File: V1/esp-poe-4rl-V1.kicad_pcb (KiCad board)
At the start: 4 copper layers, 82.5 x 45 mm, 105 parts, among them J1 USB_C_Receptacle_USB2.0, J2 250-202, J3 RJ45 JACK, J4 250-202, K1 G5NB-1A-E-DC5, K2 G5NB-1A-E-DC5, Q1 UMH3N, Q2 MMBT2222A, Q3 WPM2015-3/TR, Q4 LMUN2211LT1G, Q5 MMBT2222A, SW1 RESET, U1 CH340K, U2 ESP32-WROOM-32UE-N16, U3 LAN8710A, U4 TPS2376DDAR-H, U5 TX4138, U6 SY8089A1AAC

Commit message: Under development.
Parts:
- added D12: WHITE, Tales:LED_0603_1608Metric, F.Cu at (71.6, 59.1)
- added D13: WHITE, Tales:LED_0603_1608Metric, F.Cu at (71.6, 61.7)
- added D14: 1N4148, Tales:D_SOD-123, F.Cu at (66.7, 59.5)
- added D15: 1N4148, Tales:D_SOD-123, F.Cu at (66.7, 63.0)
- added J5: 250-203, Tales:TerminalBlock_Wago_250-203_1x03_P3.5mm_45Degree, F.Cu at (77.0, 108.0)
- added J6: 250-203, Tales:TerminalBlock_Wago_250-203_1x03_P3.5mm_45Degree, F.Cu at (90.0, 108.0)
- added K3: G5Q-14-DC5, Relay_THT:Relay_SPDT_Omron-G5Q-1, F.Cu at (72.2, 82.1)
- added K4: G5Q-14-DC5, Relay_THT:Relay_SPDT_Omron-G5Q-1, F.Cu at (85.2, 82.1)
- added Q6: MMBT2222A, Tales:SOT-23, F.Cu at (61.0, 59.6)
- added Q7: MMBT2222A, Tales:SOT-23, F.Cu at (61.0, 63.5)
- added R44: 10k, Tales:R_0402_1005Metric, F.Cu at (57.1, 58.7)
- added R45: 10k, Tales:R_0402_1005Metric, F.Cu at (57.1, 60.7)
- added R46: 1k, Tales:R_0402_1005Metric, F.Cu at (57.1, 62.7)
- added R47: 1k, Tales:R_0402_1005Metric, F.Cu at (57.1, 64.7)
- added R48: 680R, Tales:R_0402_1005Metric, F.Cu at (57.1, 66.7)
- added R49: 680R, Tales:R_0402_1005Metric, F.Cu at (57.1, 68.7)
- J2, J4: value 250-202 -> 250-203; footprint Tales:TerminalBlock_Wago_250-202_1x02_P3.5mm_45Degree -> Tales:TerminalBlock_Wago_250-203_1x03_P3.5mm_45Degree
- K1, K2: value G5NB-1A-E-DC5 -> G5Q-14-DC5; footprint Tales:Relay_SPST_Omron_G5NB-1A -> Relay_THT:Relay_SPDT_Omron-G5Q-1
- moved K1 36.1 mm to (46.2, 82.1)
- moved K2 32.6 mm to (59.2, 82.1)
- moved D3 31.5 mm to (49.0, 78.0)
- moved D4 31.5 mm to (49.5, 75.5)
- moved Q2 31.5 mm to (53.0, 77.0)
- moved R21 31.5 mm to (48.2, 74.0)
- moved R22 31.5 mm to (54.0, 74.0)
- moved R23 31.5 mm to (51.5, 74.0)
- moved J2 31.3 mm to (51.0, 108.0)
- moved J4 28.3 mm to (64.0, 108.0)
- moved D5 27.5 mm to (62.0, 78.0)
- moved D6 27.5 mm to (62.5, 75.5)
- moved Q5 27.5 mm to (66.0, 77.0)
- moved R27 27.5 mm to (61.2, 74.0)
- moved R29 27.5 mm to (67.0, 74.0)
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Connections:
- J2 pad 1: /RELAY OUTPUTS/OUT1LN -> /RELAY OUTPUTS/OUT1NC
- J2 pad 2: /RELAY OUTPUTS/OUT1LD -> /RELAY OUTPUTS/OUT1LN
- J4 pad 1: /RELAY OUTPUTS/OUT2LN -> /RELAY OUTPUTS/OUT3NC
- J4 pad 2: /RELAY OUTPUTS/OUT2LD -> /RELAY OUTPUTS/OUT3LN
- K1 pad 1: +5V -> /RELAY OUTPUTS/OUT1CMD
- K1 pad 3: /RELAY OUTPUTS/OUT1LD -> /RELAY OUTPUTS/OUT1NO
- K1 pad 4: /RELAY OUTPUTS/OUT1CMD -> /RELAY OUTPUTS/OUT1NC
- K2 pad 1: +5V -> /RELAY OUTPUTS/OUT3CMD
- K2 pad 2: /RELAY OUTPUTS/OUT2LN -> /RELAY OUTPUTS/OUT3LN
- K2 pad 3: /RELAY OUTPUTS/OUT2LD -> /RELAY OUTPUTS/OUT3NO
- K2 pad 4: /RELAY OUTPUTS/OUT2CMD -> /RELAY OUTPUTS/OUT3NC
- U2 pad 24: unconnected-(U2-IO2-Pad24) -> OUT3
- U2 pad 26: unconnected-(U2-IO4-Pad26) -> OUT4
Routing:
- net OUT2: track 37.9 -> 3.35 mm, vias 2 -> 1
- net OUT1: track 33.5 -> 1.48 mm, vias 2 -> 1
- net +5V: track 104.1 -> 86.9 mm
- net /RELAY OUTPUTS/OUT2LN: track 16.5 -> 0.00 mm
- net /RELAY OUTPUTS/OUT2LD: track 16.0 -> 0.00 mm
- net /RELAY OUTPUTS/OUT1LN: track 15.9 -> 0.00 mm
- net /RELAY OUTPUTS/OUT1LD: track 15.2 -> 0.00 mm
- net /RELAY OUTPUTS/OUT2CMD: track 9.60 -> 5.00 mm
- net /RELAY OUTPUTS/OUT1CMD: track 9.10 -> 5.00 mm

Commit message: Development
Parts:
- removed the D3 at (49.0, 78.0)
- removed the D4 at (49.5, 75.5)
- removed the D5 at (62.0, 78.0)
- removed the D6 at (62.5, 75.5)
- removed the J2 at (51.0, 108.0)
- removed the Q2 at (53.0, 77.0)
- removed the R21 at (48.2, 74.0)
- removed the R22 at (54.0, 74.0)
- removed the R23 at (51.5, 74.0)
- removed the R27 at (61.2, 74.0)
- removed the R29 at (67.0, 74.0)
- removed the R30 at (64.5, 74.0)
- added D10: WHITE, Tales:LED_0603_1608Metric, F.Cu at (46.5, 86.2)
- added D11: WHITE, Tales:LED_0603_1608Metric, F.Cu at (46.5, 88.9)
- added D8: 1N4148, Tales:D_SOD-123, F.Cu at (41.6, 86.7)
- added D9: 1N4148, Tales:D_SOD-123, F.Cu at (41.6, 90.2)
- added J3: 250-202, Tales:TerminalBlock_Wago_250-202_1x02_P3.5mm_45Degree, F.Cu at (82.0, 107.8)
- added Q4: MMBT2222A, Tales:SOT-23, F.Cu at (35.9, 86.8)
- added R38: 680R, Tales:R_0402_1005Metric, F.Cu at (34.9, 101.3)
- added R39: 680R, Tales:R_0402_1005Metric, F.Cu at (34.9, 103.3)
- added R40: 1k, Tales:R_0402_1005Metric, F.Cu at (34.9, 105.3)
- added R41: 1k, Tales:R_0402_1005Metric, F.Cu at (34.9, 107.3)
- added R42: 10k, Tales:R_0402_1005Metric, F.Cu at (37.9, 101.3)
- added R43: 10k, Tales:R_0402_1005Metric, F.Cu at (37.9, 103.3)
- D12, D13: value WHITE -> 1N4148; footprint Tales:LED_0603_1608Metric -> Tales:D_SOD-123
- D14, D15: value 1N4148 -> WHITE; footprint Tales:D_SOD-123 -> Tales:LED_0603_1608Metric
- J4, J5, J6: value 250-203 -> 250-202; footprint Tales:TerminalBlock_Wago_250-203_1x03_P3.5mm_45Degree -> Tales:TerminalBlock_Wago_250-202_1x02_P3.5mm_45Degree
- K1, K2, K3, K4: value G5Q-14-DC5 -> G5NB-1A-E-DC5; footprint Relay_THT:Relay_SPDT_Omron-G5Q-1 -> Tales:Relay_SPST_Omron_G5NB-1A
- R44, R45: value 10k -> 680R
- R48, R49: value 680R -> 10k
- moved R45 50.4 mm to (37.9, 107.3)
- moved R44 50.4 mm to (37.9, 105.3)
- moved D13 46.4 mm to (41.6, 97.1)
- moved D12 45.8 mm to (41.6, 93.7)
- moved Q6 43.0 mm to (35.9, 94.5)
- moved Q7 43.0 mm to (35.9, 98.4)
- moved R46 41.9 mm to (40.8, 101.3)
- moved R47 41.9 mm to (40.8, 103.3)
- moved R48 41.9 mm to (40.8, 105.3)
- moved R49 41.9 mm to (40.8, 107.3)
- moved D14 37.8 mm to (46.5, 91.5)
- moved D15 37.0 mm to (46.5, 94.1)
- moved K1 35.1 mm to (80.5, 89.5)
- moved Q5 33.0 mm to (35.9, 90.7), turned to 0 degrees
- moved K2 31.4 mm to (89.8, 89.5)
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- renumbered D7 to D3, D8 to D4, D9 to D5, D10 to D6, D11 to D7, J3 to J2, Q3 to Q2, Q4 to Q3, R25 to R21, R24 to R22, R28 to R23, R26 to R24, R31 to R25, R32 to R26, R33 to R27, R34 to R28, R35 to R29, R36 to R30, R37 to R31, R38 to R32, R39 to R33, R40 to R34, R41 to R35, R42 to R36, R43 to R37
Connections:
- net /RELAY OUTPUTS/OUT1BJT renamed /RELAY OUTPUTS/OUT3BJT
- D12 pad 1: /RELAY OUTPUTS/OUT3CMD -> +5V
- D12 pad 2: /RELAY OUTPUTS/OUT1ON -> /RELAY OUTPUTS/OUT3CMD
- D13 pad 1: /RELAY OUTPUTS/OUT24MD -> +5V
- D13 pad 2: /RELAY OUTPUTS/OUT2ON -> /RELAY OUTPUTS/OUT4CMD
- D14 pad 1: +5V -> /RELAY OUTPUTS/OUT3CMD
- D14 pad 2: /RELAY OUTPUTS/OUT3CMD -> /RELAY OUTPUTS/OUT3ON
- D15 pad 1: +5V -> /RELAY OUTPUTS/OUT4CMD
- D15 pad 2: /RELAY OUTPUTS/OUT24MD -> /RELAY OUTPUTS/OUT4ON
- J4 pad 1: /RELAY OUTPUTS/OUT3NC -> /RELAY OUTPUTS/OUT2LN
- J4 pad 2: /RELAY OUTPUTS/OUT3LN -> /RELAY OUTPUTS/OUT2LD
- J5 pad 1: /RELAY OUTPUTS/OUT2NC -> /RELAY OUTPUTS/OUT3LN
- J5 pad 2: /RELAY OUTPUTS/OUT2LN -> /RELAY OUTPUTS/OUT3LD
- J6 pad 1: /RELAY OUTPUTS/OUT4NC -> /RELAY OUTPUTS/OUT4LN
- J6 pad 2: /RELAY OUTPUTS/OUT4LN -> /RELAY OUTPUTS/OUT4LD
- K1 pad 1: /RELAY OUTPUTS/OUT1CMD -> +5V
- K1 pad 3: /RELAY OUTPUTS/OUT1NO -> /RELAY OUTPUTS/OUT1LD
- K1 pad 4: /RELAY OUTPUTS/OUT1NC -> /RELAY OUTPUTS/OUT1CMD
- K2 pad 1: /RELAY OUTPUTS/OUT3CMD -> +5V
- K2 pad 2: /RELAY OUTPUTS/OUT3LN -> /RELAY OUTPUTS/OUT2LN
- K2 pad 3: /RELAY OUTPUTS/OUT3NO -> /RELAY OUTPUTS/OUT2LD
- K2 pad 4: /RELAY OUTPUTS/OUT3NC -> /RELAY OUTPUTS/OUT2CMD
- K3 pad 1: /RELAY OUTPUTS/OUT2CMD -> +5V
- K3 pad 2: /RELAY OUTPUTS/OUT2LN -> /RELAY OUTPUTS/OUT3LN
- K3 pad 3: /RELAY OUTPUTS/OUT2NO -> /RELAY OUTPUTS/OUT3LD
- K3 pad 4: /RELAY OUTPUTS/OUT2NC -> /RELAY OUTPUTS/OUT3CMD
- K4 pad 1: /RELAY OUTPUTS/OUT24MD -> +5V
- K4 pad 3: /RELAY OUTPUTS/OUT4NO -> /RELAY OUTPUTS/OUT4LD
- K4 pad 4: /RELAY OUTPUTS/OUT4NC -> /RELAY OUTPUTS/OUT4CMD
- Q7 pad 1: /RELAY OUTPUTS/OUT2BJT -> /RELAY OUTPUTS/OUT4BJT
- Q7 pad 3: /RELAY OUTPUTS/OUT24MD -> /RELAY OUTPUTS/OUT4CMD
- R44 pad 1: OUT3 -> +5V
- R44 pad 2: GND -> /RELAY OUTPUTS/OUT3ON
- R45 pad 1: OUT4 -> +5V
- R45 pad 2: GND -> /RELAY OUTPUTS/OUT4ON
- R47 pad 1: /RELAY OUTPUTS/OUT2BJT -> /RELAY OUTPUTS/OUT4BJT
- R48 pad 1: +5V -> OUT3
- R48 pad 2: /RELAY OUTPUTS/OUT1ON -> GND
- R49 pad 1: +5V -> OUT4
- R49 pad 2: /RELAY OUTPUTS/OUT2ON -> GND
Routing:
- net +5V: track 86.9 -> 78.6 mm
- net GND: track 71.6 -> 66.2 mm, vias 52 -> 50
- net /RELAY OUTPUTS/OUT2CMD: track 5.00 -> 0.00 mm
- net /RELAY OUTPUTS/OUT1CMD: track 5.00 -> 0.00 mm
- net /RELAY OUTPUTS/OUT2BJT: track 2.23 -> 0.00 mm
- net /RELAY OUTPUTS/OUT3BJT: track 2.23 -> 0.00 mm
- net OUT1: track 1.48 -> 0.00 mm, vias 1 -> 0
- net OUT2: track 3.35 -> 1.87 mm, vias 1 -> 0
- net /RELAY OUTPUTS/OUT2ON: track 1.45 -> 0.00 mm
- net /RELAY OUTPUTS/OUT1ON: track 1.45 -> 0.00 mm
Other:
- board size 82.5 x 45 mm -> 99.5 x 45 mm

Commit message: V1.0.0
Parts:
- moved R45 79.7 mm to (110.0, 73.5), turned to 180 degrees
- moved R49 73.8 mm to (108.5, 78.0), turned to -90 degrees
- moved Q7 73.5 mm to (106.2, 77.0), turned to -90 degrees
- moved R47 73.0 mm to (108.5, 76.0), turned to -90 degrees
- moved D13 71.9 mm to (110.5, 76.5), turned to -90 degrees
- moved R44 70.5 mm to (100.8, 73.5), turned to 180 degrees
- moved R48 64.5 mm to (99.2, 78.0), turned to -90 degrees
- moved D15 64.3 mm to (107.5, 73.8)
- moved R39 63.9 mm to (91.5, 73.5), turned to 180 degrees
- moved R46 63.7 mm to (99.2, 76.0), turned to -90 degrees
- moved Q6 63.5 mm to (97.0, 77.0), turned to -90 degrees
- moved R41 63.3 mm to (90.0, 76.0), turned to -90 degrees
- moved D12 62.1 mm to (101.2, 76.5), turned to -90 degrees
- moved R43 58.0 mm to (90.0, 78.0), turned to -90 degrees
- moved R38 54.9 mm to (82.2, 73.5), turned to 180 degrees
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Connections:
- K1 pad 2: /RELAY OUTPUTS/OUT1LN -> /RELAY OUTPUTS/OUT1LD
- K1 pad 3: /RELAY OUTPUTS/OUT1LD -> /RELAY OUTPUTS/OUT1LN
- K2 pad 2: /RELAY OUTPUTS/OUT2LN -> /RELAY OUTPUTS/OUT2LD
- K2 pad 3: /RELAY OUTPUTS/OUT2LD -> /RELAY OUTPUTS/OUT2LN
- K3 pad 2: /RELAY OUTPUTS/OUT3LN -> /RELAY OUTPUTS/OUT3LD
- K3 pad 3: /RELAY OUTPUTS/OUT3LD -> /RELAY OUTPUTS/OUT3LN
- K4 pad 2: /RELAY OUTPUTS/OUT4LN -> /RELAY OUTPUTS/OUT4LD
- K4 pad 3: /RELAY OUTPUTS/OUT4LD -> /RELAY OUTPUTS/OUT4LN
- U2 pad 24: OUT3 -> unconnected-(U2-IO2-Pad24)
- U2 pad 26: OUT4 -> unconnected-(U2-IO4-Pad26)
- U2 pad 8: unconnected-(U2-IO32-Pad8) -> OUT4
- U2 pad 9: unconnected-(U2-IO33-Pad9) -> OUT3
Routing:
- net +5V: track 78.6 -> 168.1 mm, vias 7 -> 11
- net OUT1: track 0.00 -> 51.2 mm, vias 0 -> 2
- net OUT2: track 1.87 -> 52.8 mm, vias 0 -> 2
- net /RELAY OUTPUTS/OUT4LD: track 0.00 -> 39.6 mm
- net /RELAY OUTPUTS/OUT3LD: track 0.00 -> 39.6 mm
- net /RELAY OUTPUTS/OUT1LD: track 0.00 -> 39.6 mm
- net /RELAY OUTPUTS/OUT2LD: track 0.00 -> 39.6 mm
- net OUT3: track 0.00 -> 24.4 mm, vias 0 -> 2
- net OUT4: track 0.00 -> 15.1 mm, vias 0 -> 2
- net /RELAY OUTPUTS/OUT4CMD: track 0.00 -> 13.0 mm
- net /RELAY OUTPUTS/OUT3CMD: track 0.00 -> 13.0 mm
- net /RELAY OUTPUTS/OUT2CMD: track 0.00 -> 13.0 mm
- net /RELAY OUTPUTS/OUT1CMD: track 0.00 -> 13.0 mm
- net /RELAY OUTPUTS/OUT4LN: track 0.00 -> 12.7 mm
- net /RELAY OUTPUTS/OUT3LN: track 0.00 -> 12.7 mm
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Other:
- outline, holes or cut-outs redrawn
- board text added: "OUT3"
- board text added: "OUT4"
- board text added: "V1.0.0 2026-06-15"
- board text added: "eumesmo-poe-4rl"
- board text removed: "ESP-POE-4RL V1"
- board text removed: "V1.4.0 2026-06-10"

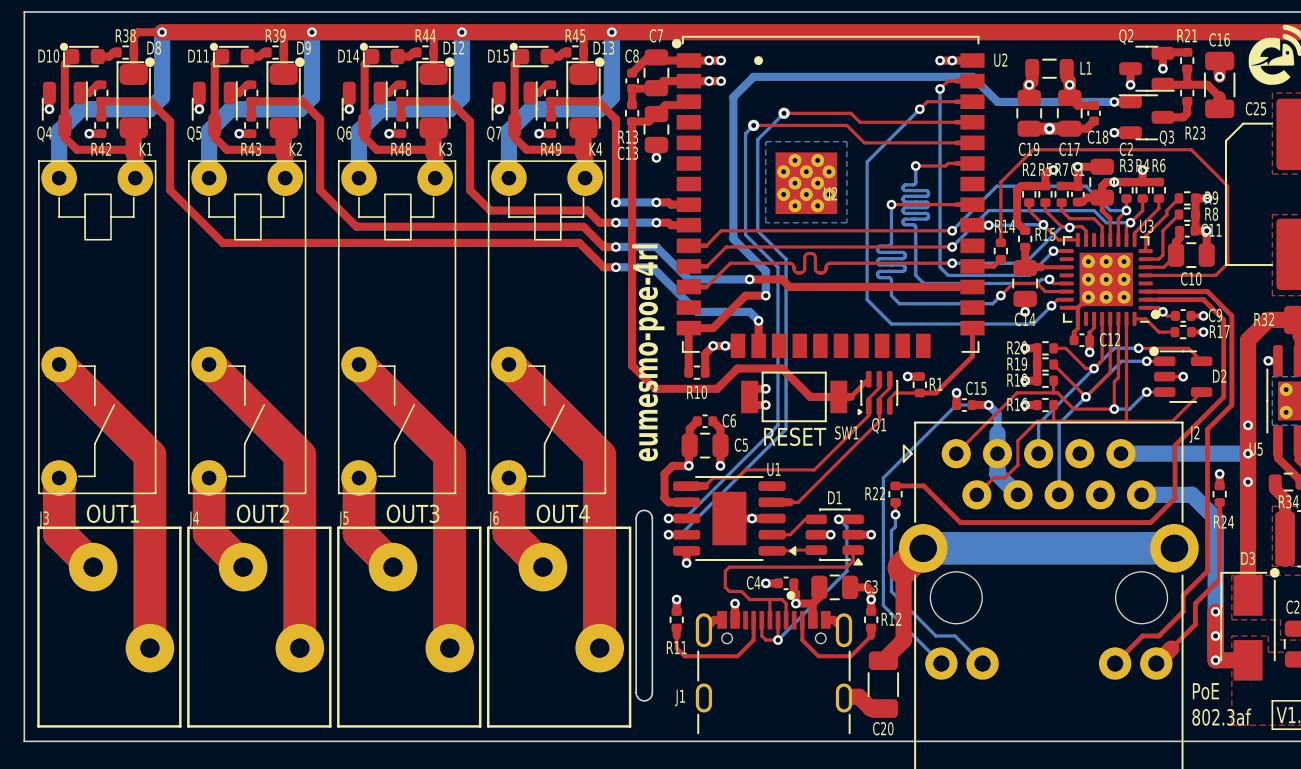
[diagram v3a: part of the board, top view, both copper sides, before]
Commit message: Adjusting traces width.
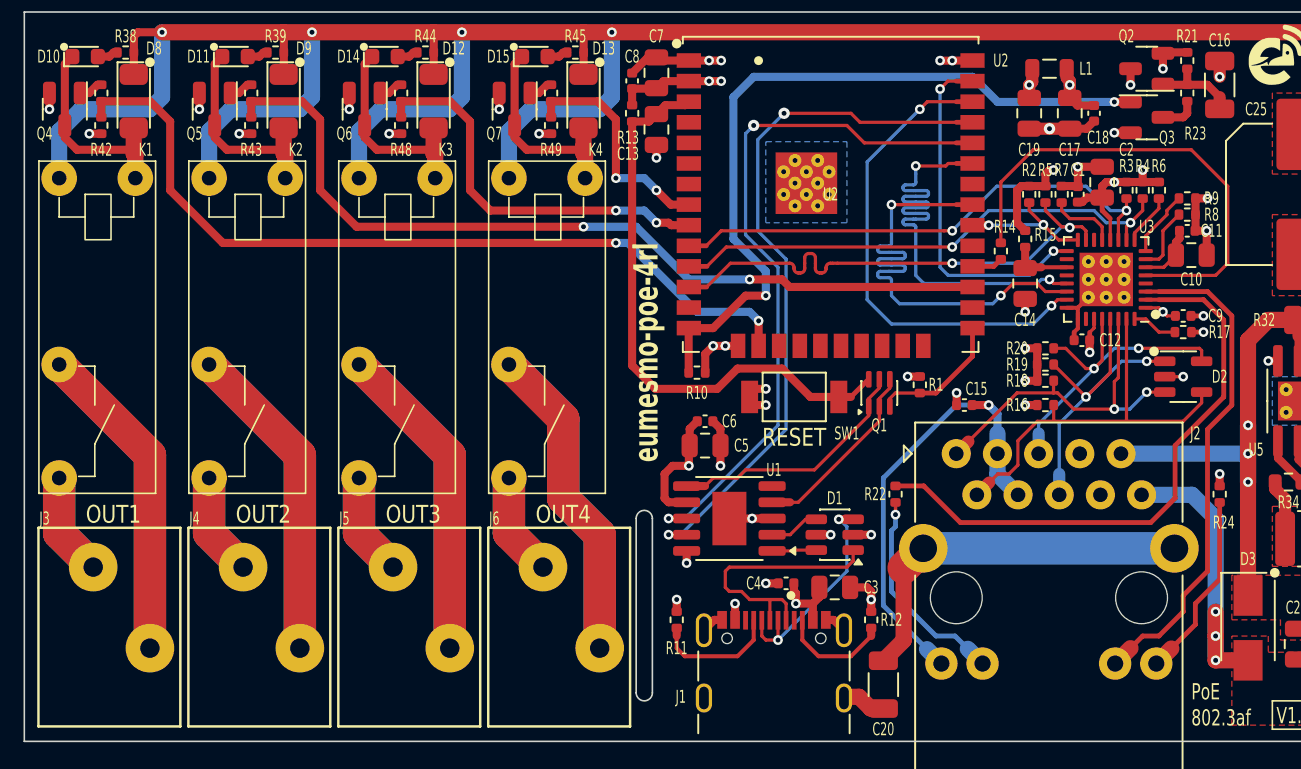
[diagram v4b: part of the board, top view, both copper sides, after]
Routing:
- net OUT4: track 15.1 -> 14.2 mm
